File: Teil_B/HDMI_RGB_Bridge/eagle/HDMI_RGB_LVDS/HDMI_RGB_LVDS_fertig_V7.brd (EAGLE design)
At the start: 70 x 60 mm, 95 parts, among them CON1 KLDX-0202-A-LT, CON2 FCI-10029449-111RLF, CON3 XF2M-4015-1A, CON4 FCI-10033526-N3212LF, CON5 MOLEX-53261-0671, CON6 FI-X30SSLA-HF, IC2 WPMDL1300331BD, IC4 AT24C01C-SSHM-B, IC5 TFP401APZP, IC6 ATMEGA88PA, IC7 FT232RL, IC8 SN75LVDS83BDGGR, Q1 ATS073ASM-1, T1 IRLML5203TRPBF, T2 IRLML2502TRPBF

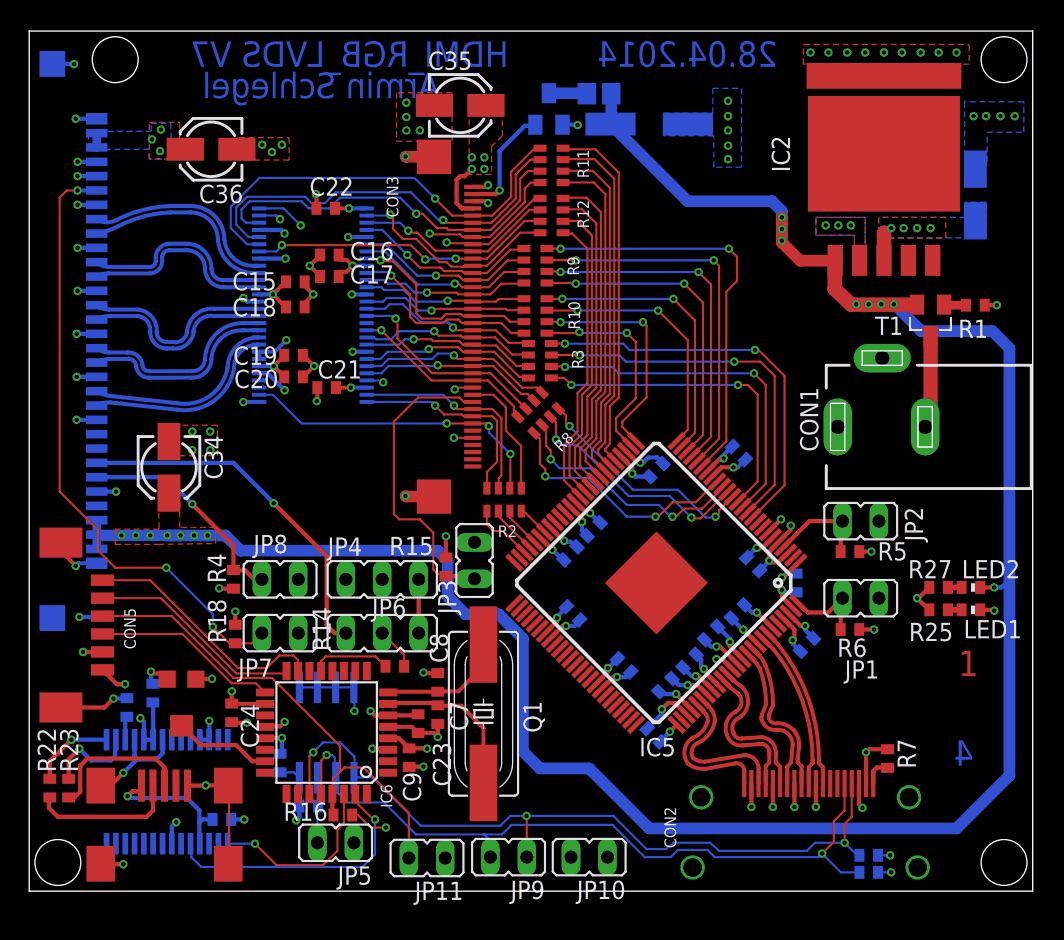
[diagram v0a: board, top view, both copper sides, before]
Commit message: reviewd lbr, changd schematics to V7
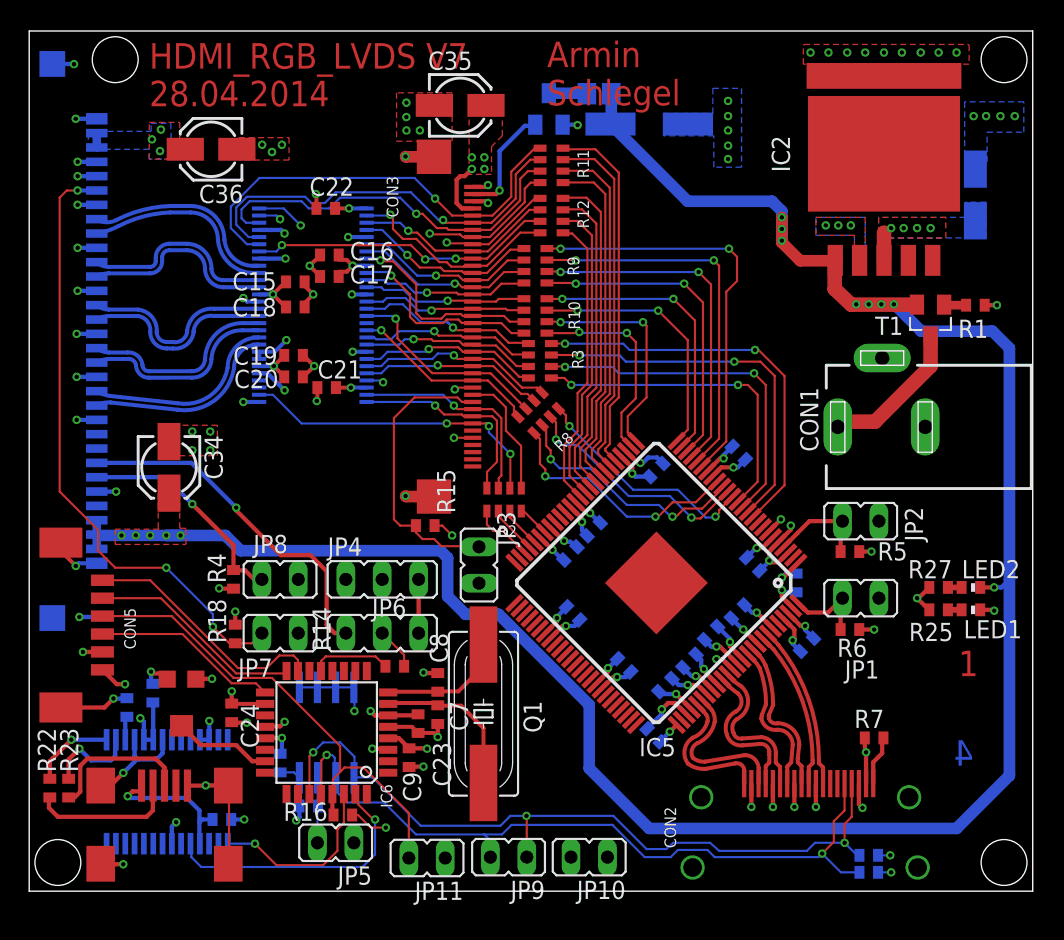
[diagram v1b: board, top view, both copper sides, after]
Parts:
- moved R15 3.21 mm to (27.6, 25.5), turned to 0 degrees
- moved R7 1.72 mm to (58.9, 10.7), turned to 180 degrees
- moved JP3 0.44 mm to (31.4, 22.8), turned to 0 degrees
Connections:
- net GND: now also CON1.3; no longer CON1.1
- net N$2: now also CON1.1; no longer CON1.3
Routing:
- net N$2: track 6.70 -> 10.3 mm
- net +12V: track 161.9 -> 160.1 mm, vias 15 -> 13
- net RGB_DISP: track 21.8 -> 20.3 mm
- net N$18: track 1.99 -> 3.48 mm
- net +5V: track 28.9 -> 28.3 mm
- net LVDS_PWM: track 25.1 -> 24.6 mm
